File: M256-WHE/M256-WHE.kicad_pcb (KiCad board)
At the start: 2 copper layers, 301.8 x 97 mm, 253 parts, among them J1 JST_SH, J2 TC2030, SW1 TS-1187A-B-A-B, SW2 TS-1187A-B-A-B, U1 USBLC6-2SC6, U2 TLV75733PDBV, U3 XC6206P332MR-G, U4 STM32F446RET6, Y1 X322516MLB4SI

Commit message: :art: adjust board outline
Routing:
- net +3.3VA: track 1741.9 -> 1741.1 mm
- net GND: vias 1503 -> 2284
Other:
- outline, holes or cut-outs redrawn

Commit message: :sparkles: new board with at32f405
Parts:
- removed J2: TC2030, Connector:Tag-Connect_TC2030-IDC-FP_2x03_P1.27mm_Vertical
- added C100: 4.7n, Capacitor_SMD:C_0402_1005Metric, B.Cu at (92.0, 64.0)
- added C101: 100n, Capacitor_SMD:C_0402_1005Metric, B.Cu at (105.4, 64.3)
- added C102: 4.7n, Capacitor_SMD:C_0402_1005Metric, B.Cu at (111.0, 64.0)
- added C103: 100n, Capacitor_SMD:C_0402_1005Metric, B.Cu at (124.5, 64.3)
- added C104: 4.7n, Capacitor_SMD:C_0402_1005Metric, B.Cu at (130.1, 64.0)
- added C105: 100n, Capacitor_SMD:C_0402_1005Metric, B.Cu at (143.5, 64.3)
- added C106: 4.7n, Capacitor_SMD:C_0402_1005Metric, B.Cu at (149.1, 64.0)
- added C107: 100n, Capacitor_SMD:C_0402_1005Metric, B.Cu at (162.6, 64.3)
- added C108: 4.7n, Capacitor_SMD:C_0402_1005Metric, B.Cu at (168.2, 64.0)
- added C109: 100n, Capacitor_SMD:C_0402_1005Metric, B.Cu at (181.6, 64.3)
- added C110: 4.7n, Capacitor_SMD:C_0402_1005Metric, B.Cu at (187.2, 64.0)
- added C111: 100n, Capacitor_SMD:C_0402_1005Metric, B.Cu at (200.7, 64.3)
- added C112: 4.7n, Capacitor_SMD:C_0402_1005Metric, B.Cu at (206.3, 64.0)
- added C113: 100n, Capacitor_SMD:C_0402_1005Metric, B.Cu at (219.7, 64.3)
- added C114: 4.7n, Capacitor_SMD:C_0402_1005Metric, B.Cu at (225.3, 64.0)
- added C115: 100n, Capacitor_SMD:C_0402_1005Metric, B.Cu at (245.9, 64.3)
- added C116: 4.7n, Capacitor_SMD:C_0402_1005Metric, B.Cu at (251.5, 64.0)
- added C117: 100n, Capacitor_SMD:C_0402_1005Metric, B.Cu at (272.1, 64.3)
- added C118: 4.7n, Capacitor_SMD:C_0402_1005Metric, B.Cu at (277.7, 64.0)
- added C119: 100n, Capacitor_SMD:C_0402_1005Metric, B.Cu at (291.1, 64.3)
- added C120: 4.7n, Capacitor_SMD:C_0402_1005Metric, B.Cu at (296.8, 64.0)
- added C121: 100n, Capacitor_SMD:C_0402_1005Metric, B.Cu at (15.4, 85.0)
- added C122: 4.7n, Capacitor_SMD:C_0402_1005Metric, B.Cu at (9.76, 85.4)
- added C123: 100n, Capacitor_SMD:C_0402_1005Metric, B.Cu at (39.2, 85.0)
- added C124: 4.7n, Capacitor_SMD:C_0402_1005Metric, B.Cu at (33.6, 85.4)
- added C125: 100n, Capacitor_SMD:C_0402_1005Metric, B.Cu at (63.0, 85.0)
- added C126: 4.7n, Capacitor_SMD:C_0402_1005Metric, B.Cu at (57.4, 85.4)
- added C127: 100n, Capacitor_SMD:C_0402_1005Metric, B.Cu at (143.9, 85.0)
- added C128: 4.7n, Capacitor_SMD:C_0402_1005Metric, B.Cu at (138.3, 85.4)
- added C129: 100n, Capacitor_SMD:C_0402_1005Metric, B.Cu at (224.9, 85.0)
- added C130: 4.7n, Capacitor_SMD:C_0402_1005Metric, B.Cu at (219.3, 85.4)
- added C131: 100n, Capacitor_SMD:C_0402_1005Metric, B.Cu at (258.2, 85.0)
- added C132: 4.7n, Capacitor_SMD:C_0402_1005Metric, B.Cu at (252.7, 85.4)
- added C133: 100n, Capacitor_SMD:C_0402_1005Metric, B.Cu at (277.3, 85.0)
- added C134: 4.7n, Capacitor_SMD:C_0402_1005Metric, B.Cu at (271.7, 85.4)
- added C135: 100n, Capacitor_SMD:C_0402_1005Metric, B.Cu at (296.4, 85.0)
- added C136: 4.7n, Capacitor_SMD:C_0402_1005Metric, B.Cu at (290.8, 85.4)
- added C137: 100n, Capacitor_SMD:C_0402_1005Metric, B.Cu at (99.7, 20.5)
- added C138: 100n, Capacitor_SMD:C_0402_1005Metric, B.Cu at (156.8, 20.5)
- added C139: 100n, Capacitor_SMD:C_0402_1005Metric, B.Cu at (85.4, 39.6)
- added C140: 100n, Capacitor_SMD:C_0402_1005Metric, B.Cu at (161.6, 39.6)
- added C141: 100n, Capacitor_SMD:C_0402_1005Metric, B.Cu at (75.8, 58.6)
- added C142: 100n, Capacitor_SMD:C_0402_1005Metric, B.Cu at (166.3, 58.6)
- added C143: 100n, Capacitor_SMD:C_0402_1005Metric, B.Cu at (66.3, 77.7)
- added C144: 100n, Capacitor_SMD:C_0402_1005Metric, B.Cu at (175.4, 77.5)
- added C145: 100n, Capacitor_SMD:C_0402_1005Metric, B.Cu at (271.1, 77.7)
- added C146: 2.2u, Capacitor_SMD:C_0603_1608Metric, B.Cu at (112.6, 33.0)
- added C147: 2.2u, Capacitor_SMD:C_0603_1608Metric, B.Cu at (109.4, 36.6)
- added C148: 1u, Capacitor_SMD:C_0603_1608Metric, B.Cu at (120.8, 33.9)
- added C149: 1u, Capacitor_SMD:C_0603_1608Metric, B.Cu at (117.6, 37.5)
- added C150: 30p, Capacitor_SMD:C_0603_1608Metric, B.Cu at (115.8, 86.8)
- added C151: 30p, Capacitor_SMD:C_0603_1608Metric, B.Cu at (109.4, 86.8)
- added C152: 100n, Capacitor_SMD:C_0402_1005Metric, B.Cu at (114.6, 84.2)
- added C153: 100n, Capacitor_SMD:C_0402_1005Metric, B.Cu at (107.6, 70.6)
- added C154: 100n, Capacitor_SMD:C_0402_1005Metric, B.Cu at (116.6, 81.2)
- added C155: 10u, Capacitor_SMD:C_0603_1608Metric, B.Cu at (119.0, 81.2)
- added C156: 100n, Capacitor_SMD:C_0402_1005Metric, B.Cu at (107.4, 85.6)
- added C157: 1u, Capacitor_SMD:C_0603_1608Metric, B.Cu at (106.8, 87.0)
- added C158: 100n, Capacitor_SMD:C_0402_1005Metric, B.Cu at (117.4, 83.0)
- added C94: 4.7n, Capacitor_SMD:C_0402_1005Metric, B.Cu at (16.9, 66.3)
- added C95: 100n, Capacitor_SMD:C_0402_1005Metric, B.Cu at (53.5, 66.0)
- added C96: 4.7n, Capacitor_SMD:C_0402_1005Metric, B.Cu at (47.9, 66.3)
- added C97: 100n, Capacitor_SMD:C_0402_1005Metric, B.Cu at (67.3, 64.3)
- added C98: 4.7n, Capacitor_SMD:C_0402_1005Metric, B.Cu at (72.9, 64.0)
- added C99: 100n, Capacitor_SMD:C_0402_1005Metric, B.Cu at (86.4, 64.3)
- C10, C12, C14, C16, C18, C2, C20, C22, C24, C26, C28, C30, C32, C34, C36, C38, C4, C40, C42, C44, C46, C48, C50, C52, C54, C56, C58, C6, C60, C62, C64, C66, C68, C70, C72, C74, C76, C8, C84, C86: value 100n -> 4.7n
- C78: value 2.2u -> 4.7n; footprint Capacitor_SMD:C_0603_1608Metric -> Capacitor_SMD:C_0402_1005Metric
- C79: value 2.2u -> 100n; footprint Capacitor_SMD:C_0603_1608Metric -> Capacitor_SMD:C_0402_1005Metric
- C80, C90: value 1u -> 4.7n; footprint Capacitor_SMD:C_0603_1608Metric -> Capacitor_SMD:C_0402_1005Metric
- C81: value 1u -> 100n; footprint Capacitor_SMD:C_0603_1608Metric -> Capacitor_SMD:C_0402_1005Metric
- C82: value 4.7u -> 4.7n; footprint Capacitor_SMD:C_0603_1608Metric -> Capacitor_SMD:C_0402_1005Metric
- C88: value 10u -> 4.7n; footprint Capacitor_SMD:C_0603_1608Metric -> Capacitor_SMD:C_0402_1005Metric
- C92: value 10p -> 4.7n
- C93: value 10p -> 100n
- HE1, HE10, HE11, HE12, HE13, HE14, HE15, HE16, HE17, HE18, HE19, HE2, HE20, HE21, HE22, HE23, HE24, HE25, HE26, HE27, HE28, HE29, HE3, HE30, HE31, HE32, HE33, HE34, HE35, HE36, HE37, HE38, HE39, HE4, HE40, HE41, HE42, HE43, HE44, HE45, HE46, HE47, HE48, HE49, HE5, HE50, HE51, HE52, HE53, HE54, HE55, HE56, HE57, HE58, HE59, HE6, HE60, HE61, HE62, HE63, HE64, HE65, HE66, HE67, HE68, HE7, HE8, HE9: value DRV5055A3QDBZR -> MT9102ET
- R1, R2: value 10k -> 12k
- U4: value STM32F446RET6 -> AT32F405RCT7
- Y1: value X322516MLB4SI -> X322512MSB4SI
- moved C33 281.2 mm to (291.1, 7.20)
- moved C34 260.9 mm to (296.8, 6.80), turned to 0 degrees
- moved C61 258.7 mm to (267.3, 26.2), turned to -90 degrees
- moved C68 255.2 mm to (44.3, 44.9), turned to 0 degrees
- moved C66 243.4 mm to (18.1, 44.9), turned to 0 degrees
- moved C67 241.8 mm to (38.7, 45.3), turned to -90 degrees
- moved C62 241.1 mm to (272.9, 25.9), turned to 0 degrees
- moved C63 235.6 mm to (291.1, 26.2), turned to -90 degrees
- moved C65 216.0 mm to (12.5, 45.3), turned to -90 degrees
- moved C92 199.1 mm to (296.8, 44.9), turned to 0 degrees
- moved C91 195.6 mm to (291.1, 45.3), turned to -90 degrees
- moved C46 176.5 mm to (115.8, 25.9), turned to 0 degrees
- moved C90 167.3 mm to (265.8, 44.9), turned to 0 degrees
- moved C64 163.6 mm to (296.4, 25.4)
- moved C89 159.4 mm to (260.2, 45.3)
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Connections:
- C10 pad 1: +3.3VA -> HE5
- C12 pad 1: +3.3VA -> HE6
- C14 pad 1: +3.3VA -> HE7
- C16 pad 1: +3.3VA -> HE8
- C18 pad 1: +3.3VA -> HE9
- C2 pad 1: +3.3VA -> HE1
- C20 pad 1: +3.3VA -> HE10
- C22 pad 1: +3.3VA -> HE11
- C24 pad 1: +3.3VA -> HE12
- C26 pad 1: +3.3VA -> HE13
- C28 pad 1: +3.3VA -> HE14
- C30 pad 1: +3.3VA -> HE15
- C32 pad 1: +3.3VA -> HE16
- C34 pad 1: +3.3VA -> HE17
- C36 pad 1: +3.3VA -> HE18
- C38 pad 1: +3.3VA -> HE19
- C4 pad 1: +3.3VA -> HE2
- C40 pad 1: +3.3VA -> HE20
- C42 pad 1: +3.3VA -> HE21
- C44 pad 1: +3.3VA -> HE22
- C46 pad 1: +3.3VA -> HE23
- C48 pad 1: +3.3VA -> HE24
- C50 pad 1: +3.3VA -> HE25
- C52 pad 1: +3.3VA -> HE26
- C54 pad 1: +3.3VA -> HE27
- C56 pad 1: +3.3VA -> HE28
- C58 pad 1: +3.3VA -> HE29
- C6 pad 1: +3.3VA -> HE3
- C60 pad 1: +3.3VA -> HE30
- C62 pad 1: +3.3VA -> HE31
- C64 pad 1: +3.3VA -> HE32
- C66 pad 1: +3.3VA -> HE33
- C68 pad 1: +3.3VA -> HE34
- C70 pad 1: +3.3VA -> HE35
- C72 pad 1: +3.3VA -> HE36
- C74 pad 1: +3.3VA -> HE37
- C76 pad 1: +3.3VA -> HE38
- C78 pad 1: +5V -> HE39
- C8 pad 1: +3.3VA -> HE4
- C80 pad 1: +5V -> HE40
- C81 pad 1: +3.3V -> +3.3VA
- C82 pad 1: /VCAP -> HE41
- C83 pad 1: +3.3V -> +3.3VA
- C84 pad 1: +3.3V -> HE42
- C85 pad 1: +3.3V -> +3.3VA
- C86 pad 1: +3.3V -> HE43
- C87 pad 1: +3.3V -> +3.3VA
- C88 pad 1: +3.3V -> HE44
- C90 pad 1: +3.3VA -> HE45
- C91 pad 1: GND -> +3.3VA
- C91 pad 2: NRST -> GND
- C92 pad 1: /RCC_OSC_IN -> HE46
- C93 pad 1: /RCC_OSC_OUT -> +3.3VA
- R2 pad 1: /BOOT1 -> GND
- R2 pad 2: GND -> Net-(U4-OTGHS1_R)
- U4 pad 14: MUX_OUT_7 -> unconnected-(U4-PA0-Pad14)
- U4 pad 15: MUX_OUT_5 -> unconnected-(U4-PA1-Pad15)
- U4 pad 16: MUX_OUT_3 -> unconnected-(U4-PA2-Pad16)
- U4 pad 17: MUX_OUT_1 -> MUX_OUT_2
- U4 pad 18: GND -> unconnected-(U4-PF4-Pad18)
- U4 pad 19: +3.3V -> unconnected-(U4-PF5-Pad19)
- U4 pad 2: MUX_SELECT_0 -> unconnected-(U4-PC13-Pad2)
- U4 pad 20: MUX_OUT_2 -> MUX_OUT_4
- U4 pad 21: MUX_OUT_4 -> MUX_OUT_6
- U4 pad 22: MUX_OUT_6 -> MUX_OUT_8
- U4 pad 23: MUX_OUT_8 -> MUX_OUT_9
- U4 pad 24: unconnected-(U4-PC4-Pad24) -> MUX_OUT_7
- U4 pad 25: unconnected-(U4-PC5-Pad25) -> MUX_OUT_5
- U4 pad 26: MUX_OUT_9 -> MUX_OUT_3
- U4 pad 27: unconnected-(U4-PB1-Pad27) -> MUX_OUT_1
- U4 pad 28: /BOOT1 -> unconnected-(U4-PB2-Pad28)
- U4 pad 29: unconnected-(U4-PB10-Pad29) -> MUX_SELECT_2
- U4 pad 3: MUX_SELECT_1 -> unconnected-(U4-PC14/LEXT_IN-Pad3)
- U4 pad 30: /VCAP -> MUX_SELECT_1
- U4 pad 32: +3.3V -> MUX_SELECT_0
- U4 pad 33: unconnected-(U4-PB12-Pad33) -> Net-(U4-OTGHS1_R)
- U4 pad 34: unconnected-(U4-PB13-Pad34) -> USB_D-
- U4 pad 35: unconnected-(U4-PB14-Pad35) -> USB_D+
- U4 pad 36: unconnected-(U4-PB15-Pad36) -> +3.3V
- U4 pad 4: MUX_SELECT_2 -> unconnected-(U4-PC15/LEXT_OUT-Pad4)
- U4 pad 44: USB_D- -> unconnected-(U4-PA11-Pad44)
- U4 pad 45: USB_D+ -> unconnected-(U4-PA12-Pad45)
- U4 pad 46: SWDIO -> unconnected-(U4-PA13-Pad46)
- U4 pad 47: GND -> unconnected-(U4-PF6-Pad47)
- U4 pad 48: +3.3V -> unconnected-(U4-PF7-Pad48)
- U4 pad 49: SWCLK -> unconnected-(U4-PA14-Pad49)
- U4 pad 5: /RCC_OSC_IN -> HEXT_IN
- U4 pad 55: SWO -> unconnected-(U4-PB3-Pad55)
- U4 pad 6: /RCC_OSC_OUT -> HEXT_OUT
- Y1 pad 1: /RCC_OSC_IN -> HEXT_IN
- Y1 pad 3: /RCC_OSC_OUT -> HEXT_OUT
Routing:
- net GND: track 181.8 -> 257.6 mm, vias 2284 -> 2336
- net +3.3V: track 229.5 -> 162.4 mm, vias 8 -> 6
- net SWO: track 55.4 -> 0.00 mm
- net SWDIO: track 54.4 -> 0.00 mm
- net SWCLK: track 51.1 -> 0.00 mm
- net +3.3VA: track 1741.1 -> 1778.6 mm
- net MUX_OUT_6: track 76.0 -> 109.5 mm
- net MUX_OUT_9: track 173.5 -> 204.7 mm
- net MUX_OUT_8: track 73.0 -> 103.1 mm
- net MUX_OUT_4: track 105.8 -> 135.0 mm
- net MUX_OUT_2: track 120.4 -> 145.9 mm
- net NRST: track 94.9 -> 72.8 mm, vias 4 -> 2
- net BOOT0: track 80.9 -> 60.3 mm, vias 0 -> 2
- net /RCC_OSC_IN: track 9.37 -> 0.00 mm
- net MUX_OUT_3: track 66.2 -> 74.5 mm
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
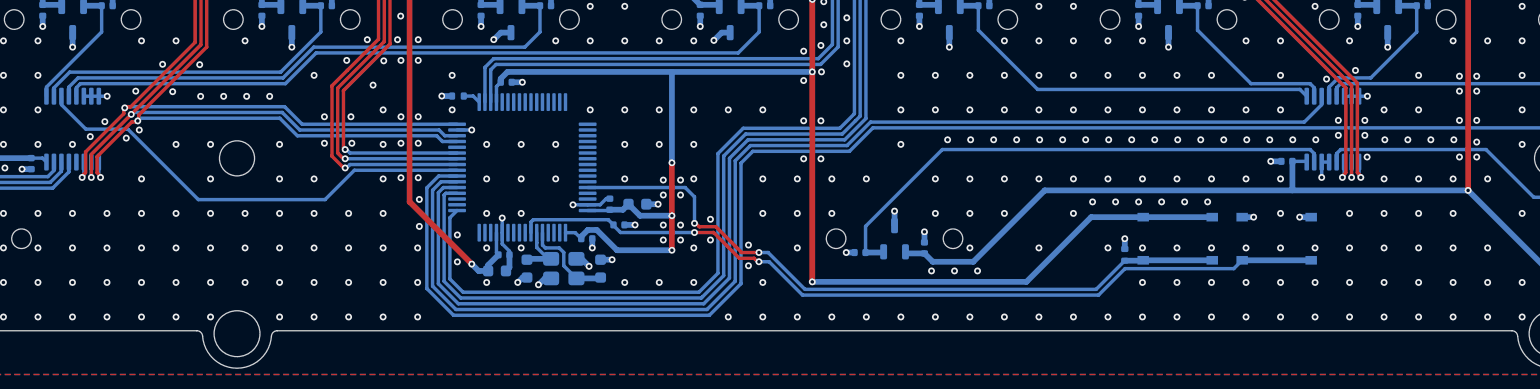
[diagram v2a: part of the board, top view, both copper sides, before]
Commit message: :sparkles: add TC2030 connector
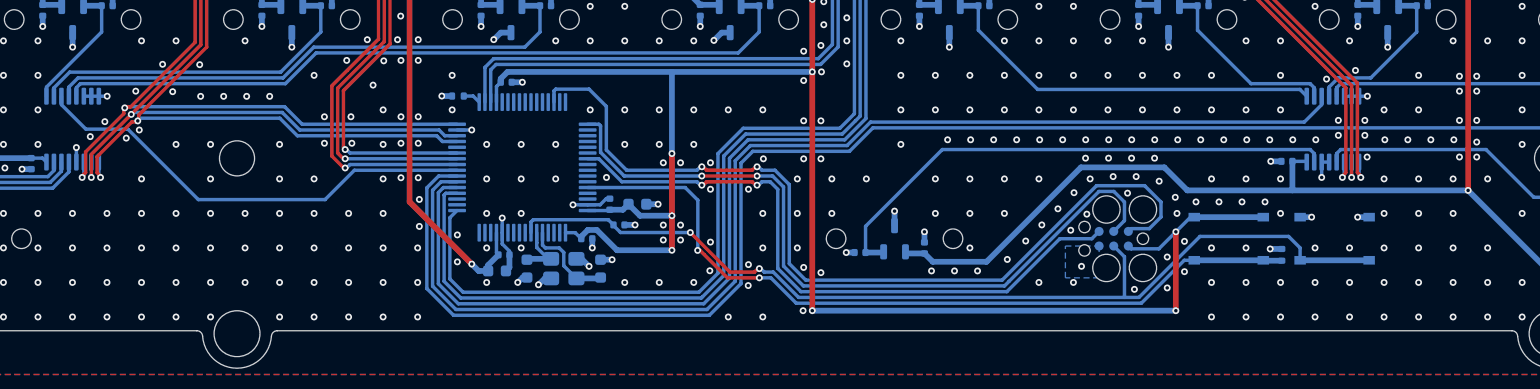
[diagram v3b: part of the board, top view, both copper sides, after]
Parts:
- added J2: TC2030, Connector:Tag-Connect_TC2030-IDC-FP_2x03_P1.27mm_Vertical, B.Cu at (160.4, 84.2)
- moved R1 13.6 mm to (175.0, 85.6)
- moved SW1 5.04 mm to (179.6, 84.2)
- moved SW2 4.44 mm to (170.4, 84.2)
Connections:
- U4 pad 46: unconnected-(U4-PA13-Pad46) -> SWDIO
- U4 pad 49: unconnected-(U4-PA14-Pad49) -> SWCLK
- U4 pad 55: unconnected-(U4-PB3-Pad55) -> SWO
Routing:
- net SWDIO: track 0.00 -> 76.1 mm, vias 0 -> 2
- net SWCLK: track 0.00 -> 64.6 mm, vias 0 -> 2
- net SWO: track 0.00 -> 55.9 mm, vias 0 -> 2
- net +3.3V: track 162.4 -> 179.2 mm, vias 6 -> 8
- net NRST: track 72.8 -> 85.5 mm
- net BOOT0: track 60.3 -> 68.6 mm
- net +3.3VA: track 1778.6 -> 1780.3 mm
- net GND: track 257.6 -> 259.0 mm
- net (no net): vias 0 -> 1
